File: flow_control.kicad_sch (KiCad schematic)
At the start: 64 parts, among them J10 Pump 1, J11 Temperature, J12 Pump 2, J13 Pump 3, J3 Flow, J7 Valve 1, J8 Valve 2, J9 Valve 3, Q1 MMBT3904, Q10 AO3401A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

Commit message: Add title to all schematics pages
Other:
- title: (none) -> Flow control
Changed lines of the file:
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@@
 	(paper "A4")
 	(title_block
+		(title "Flow control")
 		(rev "1")
 	)

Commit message: Redesign board to fit within 102mm x 102mm
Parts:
- C44, R43, U3: now left out of the parts list
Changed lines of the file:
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@@
 		(unit 1)
 		(exclude_from_sim no)
-		(in_bom yes)
+		(in_bom no)
 		(on_board yes)
 		(dnp no)
@@
 		(unit 1)
 		(exclude_from_sim no)
-		(in_bom yes)
+		(in_bom no)
 		(on_board yes)
 		(dnp no)
@@
 		(unit 1)
 		(exclude_from_sim no)
-		(in_bom yes)
+		(in_bom no)
 		(on_board yes)
 		(dnp no)

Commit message: Update max current for motor controller
Closes #8
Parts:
- R45: value 3k -> 12k; LCSC C4211 -> C22790
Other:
- note added: "I_{limit} = V_{ref}/(10 * R43) 2.5A = 2.5V/(10*0.1)"
- note removed: "I_{limit} = V_{ref}/(10 * R43) 1A = 1V/(10*0.1)"
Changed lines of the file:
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@@
 		)
 	)
-	(text "I_{limit} = V_{ref}/(10 * R43)\n1A = 1V/(10*0.1)"
+	(text "I_{limit} = V_{ref}/(10 * R43)\n2.5A = 2.5V/(10*0.1)"
 		(exclude_from_sim no)
 		(at 229.362 160.782 0)
@@
 			)
 		)
-		(property "Value" "3k"
+		(property "Value" "12k"
 			(at 201.422 151.13 0)
 			(effects
@@
 			)
 		)
-		(property "LCSC" "C4211"
+		(property "LCSC" "C22790"
 			(at 207.01 149.86 0)
 			(effects

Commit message: Swap source and drain on mosfets
Closes #4
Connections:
- net +12V: now also Q10.2 (S), Q2.2 (S), Q4.2 (S), Q6.2 (S), Q9.2 (S); no longer Q10.3 (D), Q2.3 (D), Q4.3 (D), Q6.3 (D), Q9.3 (D)
- net at D4.1 (K), J7.1 (Pin_1): now also Q2.3 (D); no longer Q2.2 (S)
- net at D7.1 (K), J13.1 (Pin_1): now also Q9.3 (D); no longer Q9.2 (S)
- net at D8.1 (K), J12.1 (Pin_1): now also Q10.3 (D); no longer Q10.2 (S)
- net at D5.1 (K), J8.1 (Pin_1): now also Q4.3 (D); no longer Q4.2 (S)
- net at D6.1 (K), J9.2 (Pin_2): now also Q6.3 (D); no longer Q6.2 (S)
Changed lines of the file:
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@@
 		(lib_id "Transistor_FET:AO3401A")
 		(at 58.42 118.11 0)
+		(mirror x)
 		(unit 1)
 		(exclude_from_sim no)
@@
 		(on_board yes)
 		(dnp no)
-		(fields_autoplaced yes)
 		(property "Reference" "Q4"
-			(at 64.77 116.8399 0)
+			(at 64.77 119.3801 0)
 			(effects
 				(font
@@
 		)
 		(property "Value" "AO3401A"
-			(at 64.77 119.3799 0)
+			(at 64.77 116.8401 0)
 			(effects
 				(font
@@
 		)
 		(property "Footprint" "Package_TO_SOT_SMD:SOT-23"
-			(at 63.5 120.015 0)
+			(at 63.5 116.205 0)
 			(effects
 				(font
@@
 		)
 		(property "Datasheet" "http://www.aosmd.com/pdfs/datasheet/AO3401A.pdf"
-			(at 63.5 121.92 0)
+			(at 63.5 114.3 0)
 			(effects
 				(font
@@
 		(lib_id "Transistor_FET:AO3401A")
 		(at 58.42 167.64 0)
+		(mirror x)
 		(unit 1)
 		(exclude_from_sim no)
@@
 		(on_board yes)
 		(dnp no)
-		(fields_autoplaced yes)
 		(property "Reference" "Q2"
-			(at 64.77 166.3699 0)
+			(at 64.77 168.9101 0)
 			(effects
 				(font
@@
 		)
 		(property "Value" "AO3401A"
-			(at 64.77 168.9099 0)
+			(at 64.77 166.3701 0)
 			(effects
 				(font
@@
 		)
 		(property "Footprint" "Package_TO_SOT_SMD:SOT-23"
-			(at 63.5 169.545 0)
+			(at 63.5 165.735 0)
 			(effects
 				(font
@@
 		)
 		(property "Datasheet" "http://www.aosmd.com/pdfs/datasheet/AO3401A.pdf"
-			(at 63.5 171.45 0)
+			(at 63.5 163.83 0)
 			(effects
 				(font
@@
 		(lib_id "Transistor_FET:AO3401A")
 		(at 130.81 118.11 0)
+		(mirror x)
 		(unit 1)
 		(exclude_from_sim no)
@@
 		(on_board yes)
 		(dnp no)
-		(fields_autoplaced yes)
 		(property "Reference" "Q9"
-			(at 137.16 116.8399 0)
+			(at 137.16 119.3801 0)
 			(effects
 				(font
@@
 		)
 		(property "Value" "AO3401A"
-			(at 137.16 119.3799 0)
+			(at 137.16 116.8401 0)
 			(effects
 				(font
@@
 		)
 		(property "Footprint" "Package_TO_SOT_SMD:SOT-23"
-			(at 135.89 120.015 0)
+			(at 135.89 116.205 0)
 			(effects
 				(font
@@
 		)
 		(property "Datasheet" "http://www.aosmd.com/pdfs/datasheet/AO3401A.pdf"
-			(at 135.89 121.92 0)
+			(at 135.89 114.3 0)
 			(effects
 				(font
@@
 		(lib_id "Transistor_FET:AO3401A")
 		(at 58.42 68.58 0)
+		(mirror x)
 		(unit 1)
 		(exclude_from_sim no)
@@
 		(dnp no)
 		(property "Reference" "Q6"
-			(at 64.77 67.3099 0)
+			(at 64.77 69.8501 0)
 			(effects
 				(font
@@
 		)
 		(property "Value" "AO3401A"
-			(at 63.246 70.104 0)
+			(at 63.246 67.056 0)
 			(effects
 				(font
@@
 		)
 		(property "Footprint" "Package_TO_SOT_SMD:SOT-23"
-			(at 63.5 70.485 0)
+			(at 63.5 66.675 0)
 			(effects
 				(font
@@
 		)
 		(property "Datasheet" "http://www.aosmd.com/pdfs/datasheet/AO3401A.pdf"
-			(at 63.5 72.39 0)
+			(at 63.5 64.77 0)
 			(effects
 				(font
@@
 		(lib_id "Transistor_FET:AO3401A")
 		(at 130.81 167.64 0)
+		(mirror x)
 		(unit 1)
 		(exclude_from_sim no)
@@
 		(on_board yes)
 		(dnp no)
-		(fields_autoplaced yes)
 		(property "Reference" "Q10"
-			(at 137.16 166.3699 0)
+			(at 137.16 168.9101 0)
 			(effects
 				(font
@@
 		)
 		(property "Value" "AO3401A"
-			(at 137.16 168.9099 0)
+			(at 137.16 166.3701 0)
 			(effects
 				(font
@@
 		)
 		(property "Footprint" "Package_TO_SOT_SMD:SOT-23"
-			(at 135.89 169.545 0)
+			(at 135.89 165.735 0)
 			(effects
 				(font
@@
 		)
 		(property "Datasheet" "http://www.aosmd.com/pdfs/datasheet/AO3401A.pdf"
-			(at 135.89 171.45 0)
+			(at 135.89 163.83 0)
 			(effects
 				(font

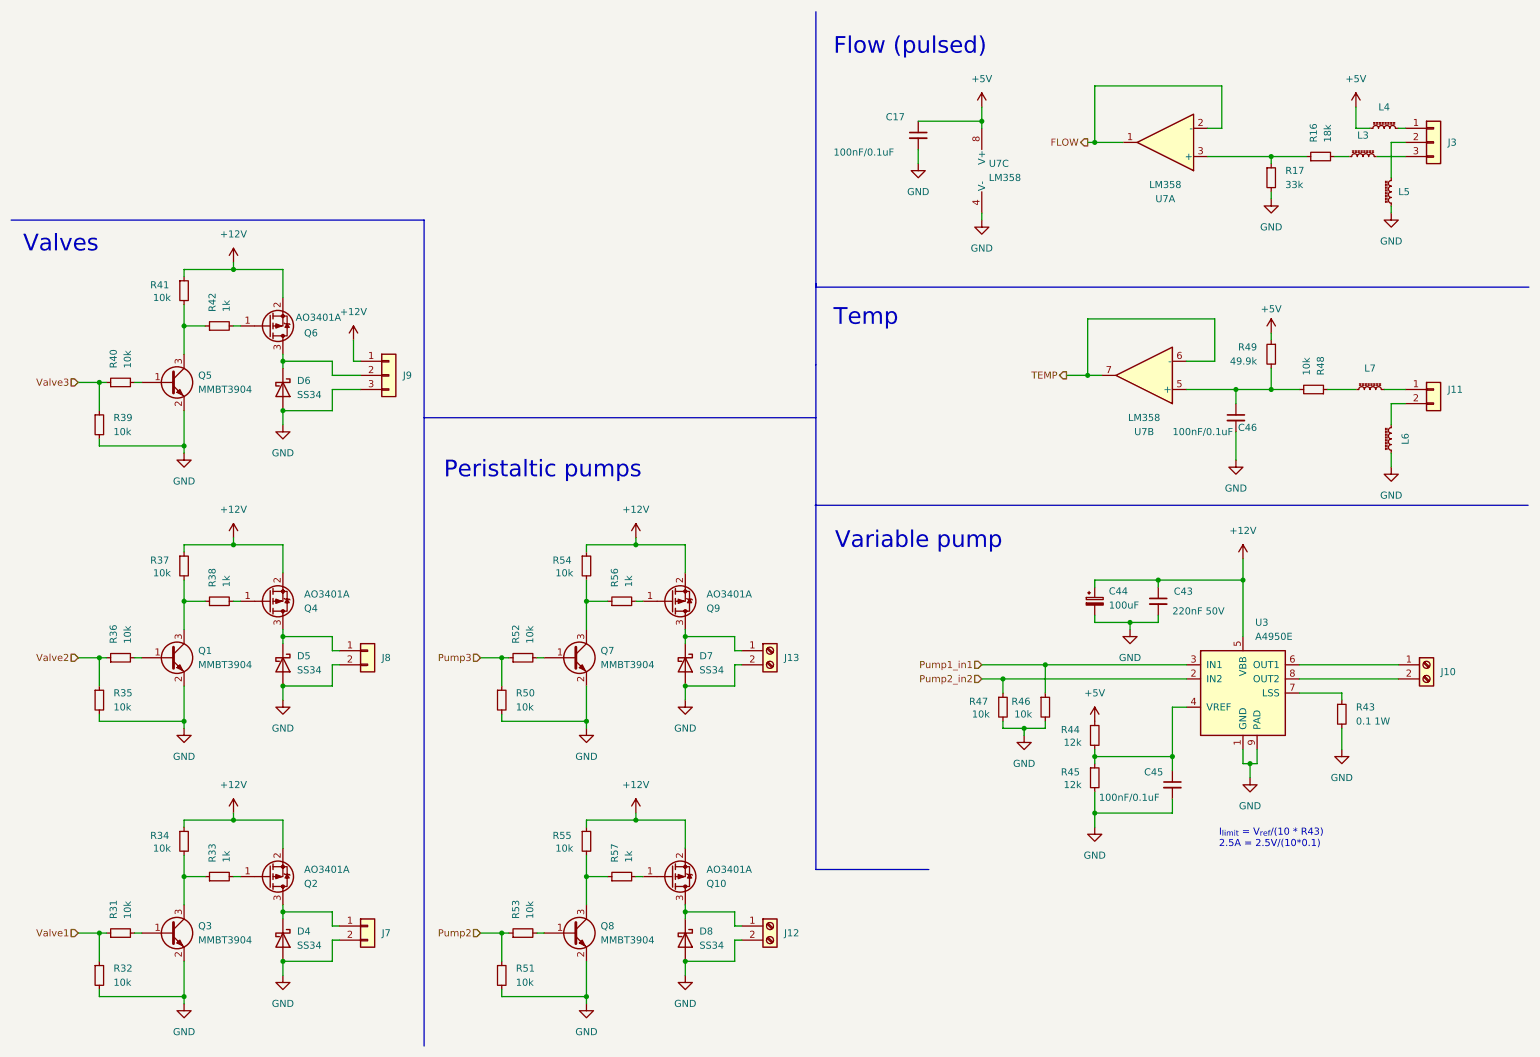
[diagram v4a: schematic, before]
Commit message: Replace motor controller with mosfets instead
Closes #21
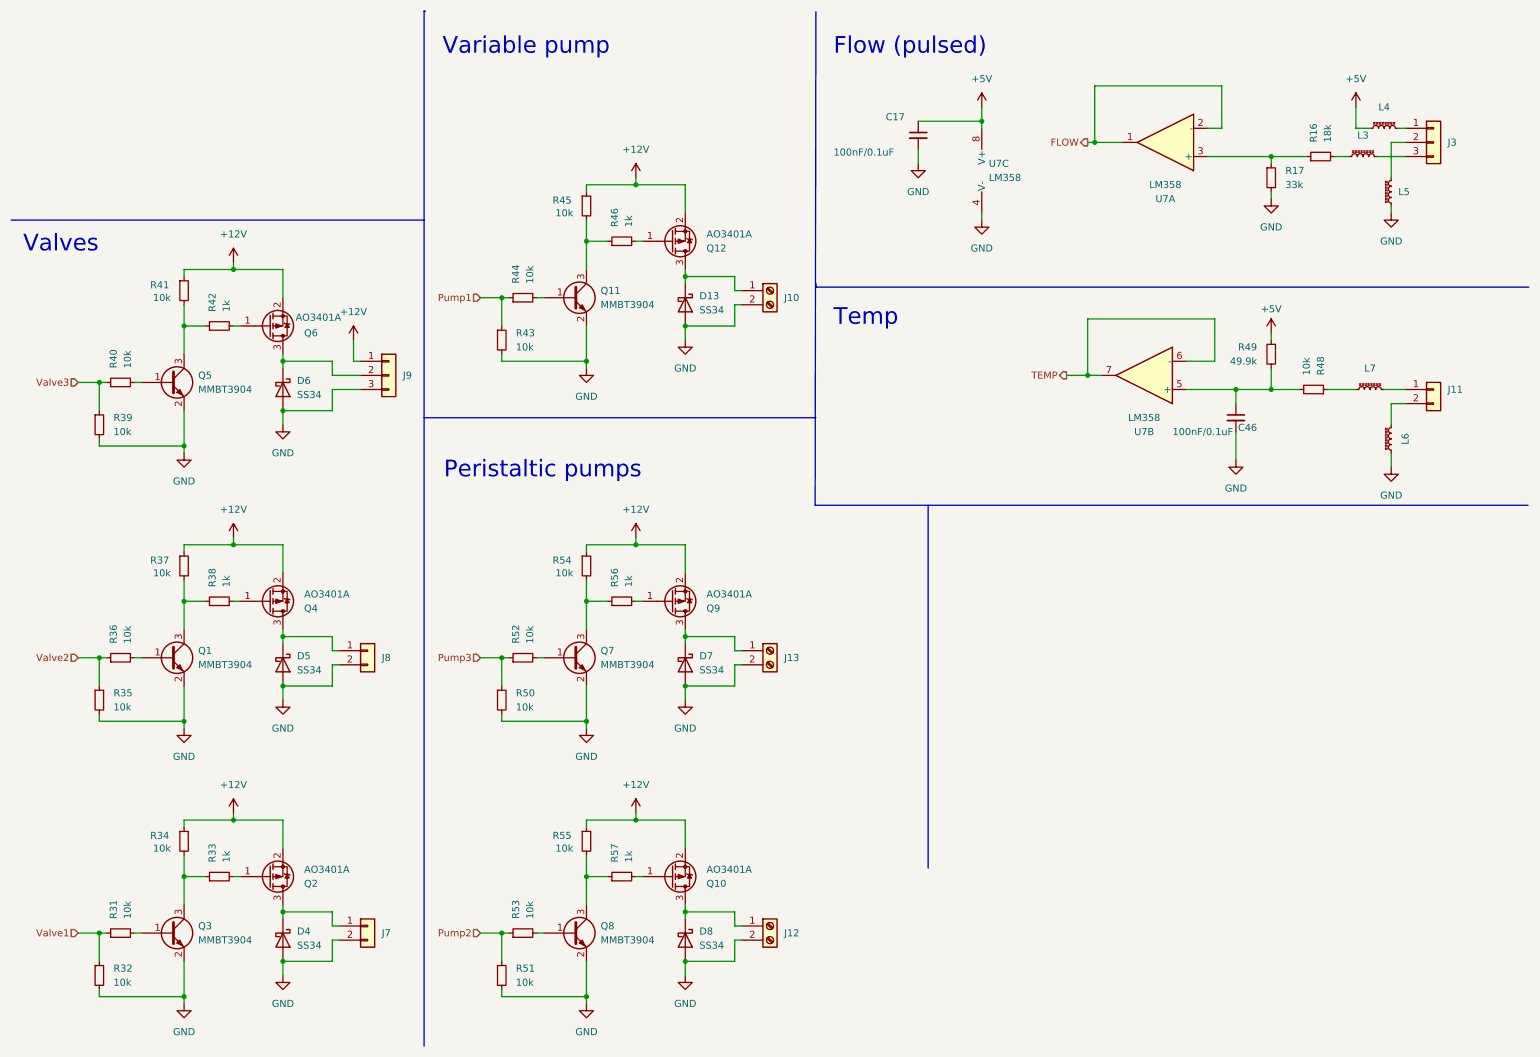
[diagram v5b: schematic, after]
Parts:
- removed C43: 220nF 50V, Capacitor_SMD:C_0805_2012Metric, symbol Device:C_Small
- removed C44: 100uF, Capacitor_SMD:CP_Elec_8x10, symbol Device:C_Polarized_Small
- removed C45: 100nF/0.1uF, Capacitor_SMD:C_0603_1608Metric, symbol Device:C_Small
- removed R47: 10k, Resistor_SMD:R_0603_1608Metric, symbol Device:R_Small
- removed U3: A4950E, Package_SO:SOIC-8-1EP_3.9x4.9mm_P1.27mm_EP2.41x3.3mm, symbol Driver_Motor:A4950E
- added D13: SS34, Diode_SMD:D_SMA, symbol Diode:SS34
- added Q11: MMBT3904, Package_TO_SOT_SMD:SOT-23, symbol Transistor_BJT:MMBT3904
- added Q12: AO3401A, Package_TO_SOT_SMD:SOT-23, symbol Transistor_FET:AO3401A
- R43: value 0.1 1W -> 10k; footprint Resistor_SMD:R_2512_6332Metric -> Resistor_SMD:R_0603_1608Metric; LCSC C2907566 -> C25804; now in the parts list
- R44, R45: value 12k -> 10k; LCSC C22790 -> C25804
- R46: value 10k -> 1k; LCSC C25804 -> C21190
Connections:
- net +12V: now also R45.1, Q12.2 (S)
- net +5V: no longer R44.1
- net GND: now also J10.2 (Pin_2), D13.2 (A), Q11.2 (E); no longer R45.2, R46.2
- net Pump1: now reaches R43.1
- net Pump1: now also R44.1
- net at R44.2: now also Q11.1 (B); no longer R45.1
- net at J10.1 (Pin_1): now also D13.1 (K), Q12.3 (D)
- net Pump1_in1: no longer names the net of R46.1
- net Pump1_in1: now also R45.2, Q11.3 (C)
- new net: Q12.1 (G), R46.2
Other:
- note removed: "I_{limit} = V_{ref}/(10 * R43) 2.5A = 2.5V/(10*0.1)"
- moved on the sheet: J10

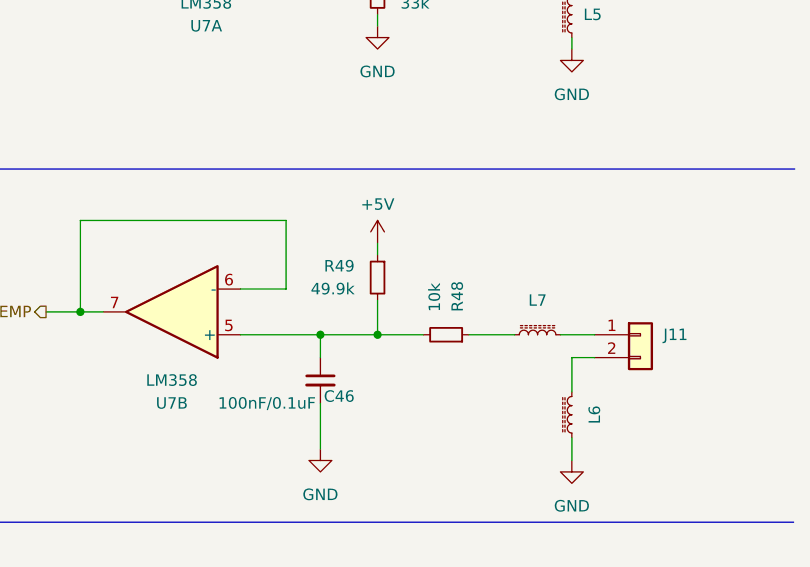
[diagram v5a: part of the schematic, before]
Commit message: Move R15 and R48 to the right side of the divider
Closes #6
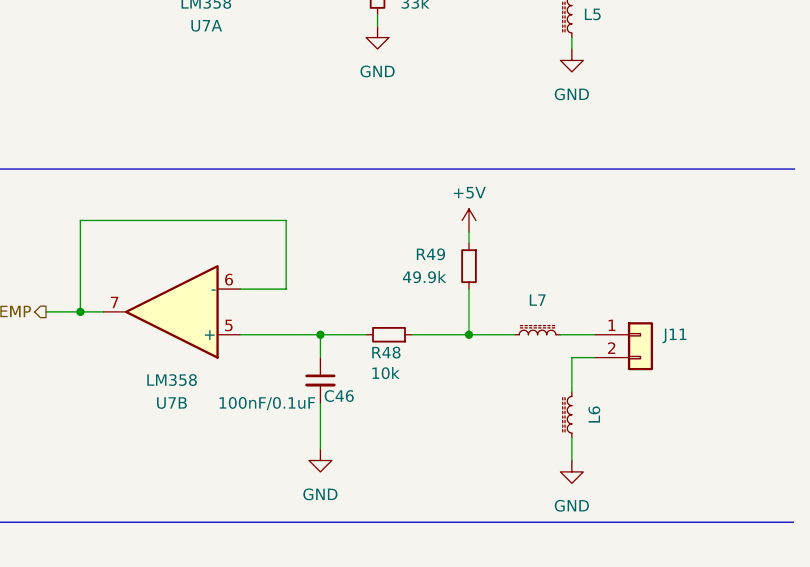
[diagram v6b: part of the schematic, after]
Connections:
- net at L7.2, R48.1: now also R49.2
- net at C46.1, R48.2, U7.5 (+): no longer R49.2
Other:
- moved on the sheet: R48, R49
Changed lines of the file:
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@@
 	)
 	(junction
+		(at 248.92 80.01)
+		(diameter 0)
+		(color 0 0 0 0)
+	)
+	(junction
 		(at 115.57 118.11)
 		(diameter 0)
@@
 		(color 0 0 0 0)
 	)
-	(junction
-		(at 238.76 80.01)
-		(diameter 0)
-		(color 0 0 0 0)
-	)
 	(wire
 		(pts
@@
 	(wire
 		(pts
+			(xy 248.92 74.93) (xy 248.92 80.01)
+		)
+		(stroke
+			(width 0)
+			(type default)
+		)
+	)
+	(wire
+		(pts
 			(xy 186.69 31.75) (xy 186.69 33.02)
 		)
@@
 	(wire
 		(pts
-			(xy 243.84 80.01) (xy 238.76 80.01)
-		)
-		(stroke
-			(width 0)
-			(type default)
-		)
-	)
-	(wire
-		(pts
 			(xy 124.46 107.95) (xy 133.35 107.95)
 		)
@@
 	(wire
 		(pts
+			(xy 248.92 80.01) (xy 254 80.01)
+		)
+		(stroke
+			(width 0)
+			(type default)
+		)
+	)
+	(wire
+		(pts
 			(xy 260.35 91.44) (xy 260.35 93.98)
 		)
@@
 	(wire
 		(pts
-			(xy 254 80.01) (xy 248.92 80.01)
-		)
-		(stroke
-			(width 0)
-			(type default)
-		)
-	)
-	(wire
-		(pts
 			(xy 142.24 124.46) (xy 133.35 124.46)
 		)
@@
 	(wire
 		(pts
-			(xy 238.76 69.85) (xy 238.76 71.12)
+			(xy 248.92 68.58) (xy 248.92 69.85)
 		)
 		(stroke
@@
 	(wire
 		(pts
-			(xy 238.76 80.01) (xy 238.76 76.2)
-		)
-		(stroke
-			(width 0)
-			(type default)
-		)
-	)
-	(wire
-		(pts
 			(xy 133.35 43.18) (xy 133.35 48.26)
 		)
@@
 	(wire
 		(pts
-			(xy 238.76 80.01) (xy 232.41 80.01)
+			(xy 232.41 80.01) (xy 237.49 80.01)
 		)
 		(stroke
@@
 	(wire
 		(pts
+			(xy 248.92 80.01) (xy 242.57 80.01)
+		)
+		(stroke
+			(width 0)
+			(type default)
+		)
+	)
+	(wire
+		(pts
 			(xy 115.57 44.45) (xy 115.57 43.18)
 		)
@@
 	(symbol
 		(lib_id "Device:R_Small")
-		(at 246.38 80.01 270)
+		(at 240.03 80.01 270)
 		(mirror x)
 		(unit 1)
@@
 		(dnp no)
 		(property "Reference" "R48"
-			(at 247.6501 77.47 0)
+			(at 237.998 82.042 90)
 			(effects
 				(font
@@
 		)
 		(property "Value" "10k"
-			(at 245.1101 77.47 0)
+			(at 237.998 84.328 90)
 			(effects
 				(font
@@
 		)
 		(property "Footprint" "Resistor_SMD:R_0603_1608Metric"
-			(at 246.38 80.01 0)
+			(at 240.03 80.01 0)
 			(effects
 				(font
@@
 		)
 		(property "Datasheet" "~"
-			(at 246.38 80.01 0)
+			(at 240.03 80.01 0)
 			(effects
 				(font
@@
 		)
 		(property "Description" "Resistor, small symbol"
-			(at 246.38 80.01 0)
+			(at 240.03 80.01 0)
 			(effects
 				(font
@@
 		)
 		(property "LCSC alt" ""
-			(at 246.38 80.01 0)
+			(at 240.03 80.01 0)
 			(effects
 				(font
@@
 		)
 		(property "LCSC" "C25804"
-			(at 246.38 80.01 0)
+			(at 240.03 80.01 0)
 			(effects
 				(font
@@
 	(symbol
 		(lib_id "Device:R_Small")
-		(at 238.76 73.66 0)
+		(at 248.92 72.39 0)
 		(mirror y)
 		(unit 1)
@@
 		(dnp no)
 		(property "Reference" "R49"
-			(at 236.22 72.3899 0)
+			(at 246.38 71.1199 0)
 			(effects
 				(font
@@
 		)
 		(property "Value" "49.9k"
-			(at 236.22 74.9299 0)
+			(at 246.38 73.6599 0)
 			(effects
 				(font
@@
 		)
 		(property "Footprint" "Resistor_SMD:R_0603_1608Metric"
-			(at 238.76 73.66 0)
+			(at 248.92 72.39 0)
 			(effects
 				(font
@@
 		)
 		(property "Datasheet" "~"
-			(at 238.76 73.66 0)
+			(at 248.92 72.39 0)
 			(effects
 				(font
@@
 		)
 		(property "Description" "Resistor, small symbol"
-			(at 238.76 73.66 0)
+			(at 248.92 72.39 0)
 			(effects
 				(font
@@
 		)
 		(property "LCSC alt" ""
-			(at 238.76 73.66 0)
+			(at 248.92 72.39 0)
 			(effects
 				(font
@@
 		)
 		(property "LCSC" "C23184"
-			(at 238.76 73.66 0)
+			(at 248.92 72.39 0)
 			(effects
 				(font
@@
 	(symbol
 		(lib_id "power:+5V")
-		(at 238.76 69.85 0)
+		(at 248.92 68.58 0)
 		(unit 1)
 		(exclude_from_sim no)
@@
 		(dnp no)
 		(property "Reference" "#PWR0117"
-			(at 238.76 73.66 0)
+			(at 248.92 72.39 0)
 			(effects
 				(font
@@
 		)
 		(property "Value" "+5V"
-			(at 238.76 65.532 0)
+			(at 248.92 64.262 0)
 			(effects
 				(font
@@
 		)
 		(property "Footprint" ""
-			(at 238.76 69.85 0)
+			(at 248.92 68.58 0)
 			(effects
 				(font
@@
 		)
 		(property "Datasheet" ""
-			(at 238.76 69.85 0)
+			(at 248.92 68.58 0)
 			(effects
 				(font
@@
 		)
 		(property "Description" "Power symbol creates a global label with name \"+5V\""
-			(at 238.76 69.85 0)
+			(at 248.92 68.58 0)
 			(effects
 				(font
